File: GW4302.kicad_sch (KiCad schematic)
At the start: 75 parts, among them J1 C64, J2 microUSB, J3 JTAG, Q1 2N3904, U1 74AHC245PW, U10 74AHC125PW, U13 CH340G, U2 74AHC245PW, U3 LD1117S33, U4 74AHC245PW, U5 74AHC245PW, U6 74AHC125PW, U8 LCMXO2-640-TG100, U9 W9825G6KH-6, Y1 12M

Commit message: RFC
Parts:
- removed Q1: 2N3904, stdpads:SOT-23, symbol Transistor_BJT:MMBT3904
- R15, R4: value 10k -> 1k; LCSC Part C25804 -> C21190
- R16: value 1k -> 10k; LCSC Part C21190 -> C25804
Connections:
- net +3V3: now also U10.12 (4A); no longer R3.1
- net GND: now also R3.2; no longer U10.12 (4A), U10.13 (4~{OE})
- net JTAG~{OE}: now also R3.1, U10.11 (4Y); no longer R3.2
- net at C34.1, R16.1, R2.1: now also U10.13 (4~{OE})
- no-connect marks 10 -> 9
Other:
- title: GW4301A -> GW4302A
- moved on the sheet: C34, R2, R5, R8, U10

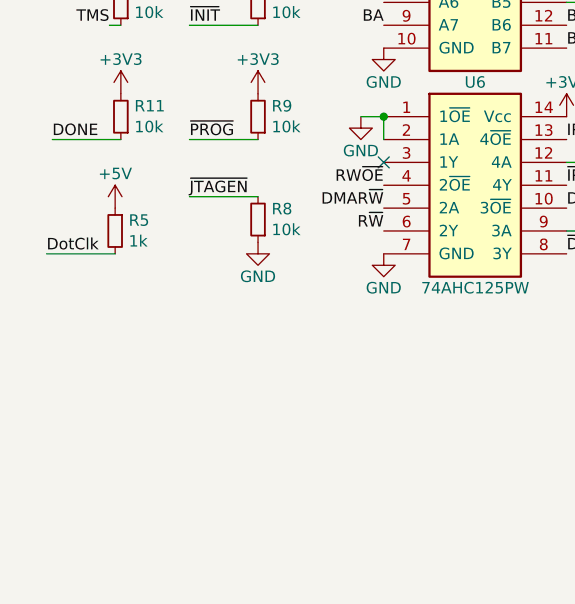
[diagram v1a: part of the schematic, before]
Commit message: Add pull-up resistors on AOE, DOE, IRQOE, RESOE
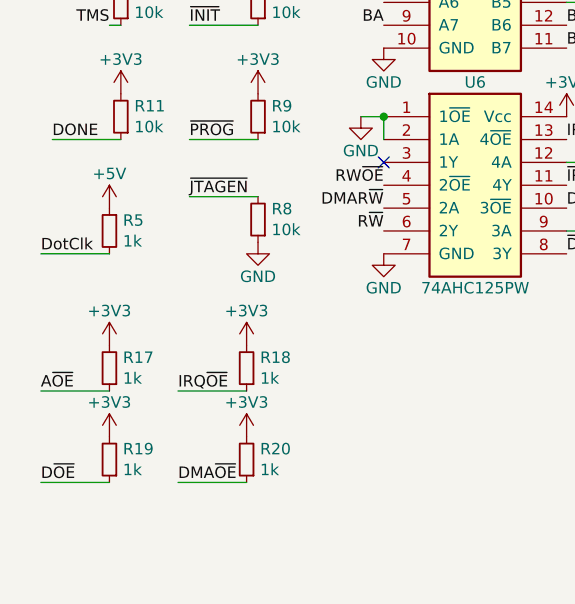
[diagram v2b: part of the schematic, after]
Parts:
- added R17, R18, R19, R20: 1k, stdpads:R_0603, symbol Device:R_Small
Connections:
- net +3V3: now also R17.2, R18.2, R19.2, R20.2
- net A~{OE}: now also R17.1
- net DMA~{OE}: now also R20.1
- net D~{OE}: now also R19.1
- net IRQ~{OE}: now also R18.1
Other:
- moved on the sheet: R5

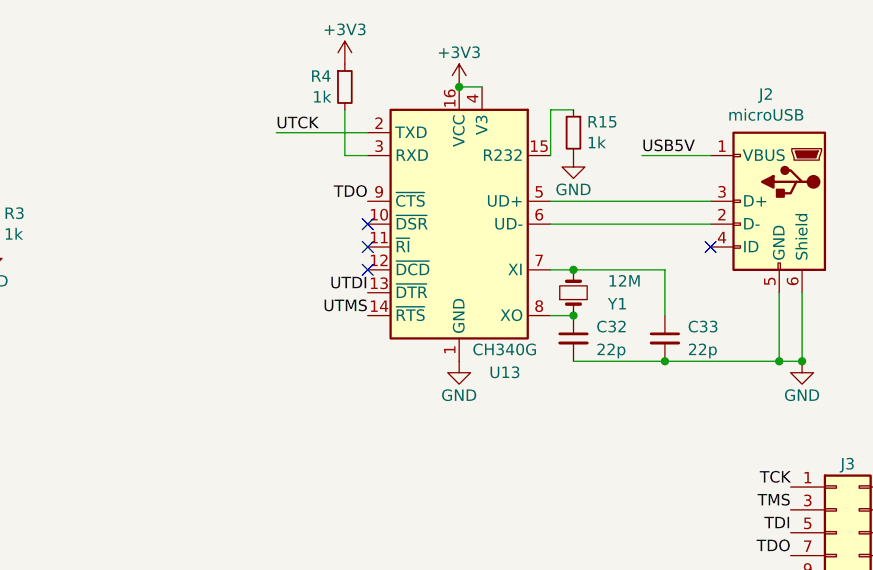
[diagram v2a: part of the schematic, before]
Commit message: Switch to 3225 crystal for USB
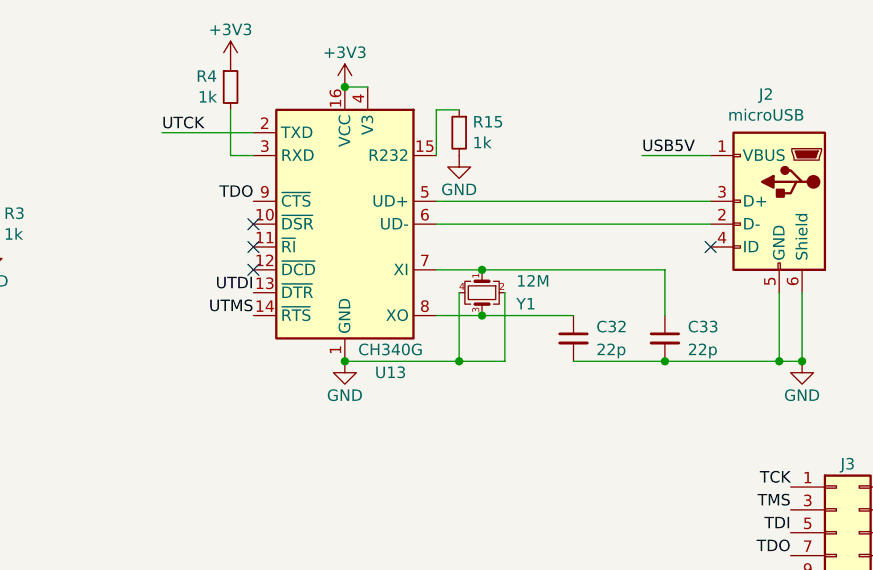
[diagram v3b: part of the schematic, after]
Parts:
- removed Y1: 12M, stdpads:Crystal_HC49-SMD, symbol Device:Crystal_Small
- added Y1: 12M, stdpads:Crystal_SMD_3225-4Pin_3.2x2.5mm, symbol Device:Crystal_GND24_Small
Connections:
- net GND: now also Y1.2, Y1.4
- net at C32.1, U13.8 (XO): now also Y1.3
- net at C33.1, U13.7 (XI): now also Y1.1
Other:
- moved on the sheet: R15, R4, U13

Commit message: Fix board ID
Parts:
- added D1: LED, stdpads:LED_0805, symbol Device:LED_Small_Filled
- added R21, R23: 1k, stdpads:R_0603, symbol Device:R_Small
- added R22: 220, stdpads:R_0805, symbol Device:R_Small
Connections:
- net +3V3: now also R21.2, R22.1, R23.1
- net RW~{OE}: now also R21.1
- net ~{LED}: now reaches U8.24 (PL7C)
- net ~{LED}: now also D1.1 (K)
- net at U13.10 (~{DSR}): now also U13.11 (~{RI}), U13.12 (~{DCD}), R23.2
- new net: D1.2 (A), R22.2
- no-connect marks 9 -> 5
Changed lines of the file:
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@@
   (junction (at 248.92 100.33) (diameter 0) (color 0 0 0 0)
   )
+  (junction (at 176.53 39.37) (diameter 0) (color 0 0 0 0)
+  )
   (junction (at 116.84 34.29) (diameter 0) (color 0 0 0 0)
   )
@@
   (junction (at 128.27 198.12) (diameter 0) (color 0 0 0 0)
   )
+  (junction (at 176.53 41.91) (diameter 0) (color 0 0 0 0)
+  )
   (junction (at 222.25 52.07) (diameter 0) (color 0 0 0 0)
   )
   (junction (at 120.65 76.2) (diameter 0) (color 0 0 0 0)
   )
-  (no_connect (at 176.53 36.83))
   (no_connect (at 50.8 156.21))
   (no_connect (at 248.92 73.66))
-  (no_connect (at 176.53 41.91))
-  (no_connect (at 176.53 39.37))
-  (no_connect (at 96.52 132.08))
   (no_connect (at 236.22 76.2))
   (no_connect (at 227.33 39.37))
@@
     (stroke (width 0) (type default) (color 0 0 0 0))
   )
+  (wire (pts (xy 151.13 64.77) (xy 153.67 64.77))
+    (stroke (width 0) (type default) (color 0 0 0 0))
+  )
   (wire (pts (xy 95.25 36.83) (xy 96.52 36.83))
     (stroke (width 0) (type default) (color 0 0 0 0))
   )
+  (wire (pts (xy 176.53 41.91) (xy 176.53 39.37))
+    (stroke (width 0) (type default) (color 0 0 0 0))
+  )
   (wire (pts (xy 218.44 130.81) (xy 228.6 130.81))
     (stroke (width 0) (type default) (color 0 0 0 0))
@@
     (stroke (width 0) (type default) (color 0 0 0 0))
   )
+  (wire (pts (xy 43.18 191.77) (xy 50.8 191.77))
+    (stroke (width 0) (type default) (color 0 0 0 0))
+  )
   (wire (pts (xy 114.3 34.29) (xy 116.84 34.29))
     (stroke (width 0) (type default) (color 0 0 0 0))
@@
     (stroke (width 0) (type default) (color 0 0 0 0))
   )
+  (wire (pts (xy 135.89 64.77) (xy 140.97 64.77))
+    (stroke (width 0) (type default) (color 0 0 0 0))
+  )
   (wire (pts (xy 204.47 44.45) (xy 204.47 52.07))
     (stroke (width 0) (type default) (color 0 0 0 0))
@@
     (stroke (width 0) (type default) (color 0 0 0 0))
   )
+  (wire (pts (xy 170.18 41.91) (xy 176.53 41.91))
+    (stroke (width 0) (type default) (color 0 0 0 0))
+  )
   (wire (pts (xy 12.7 191.77) (xy 20.32 191.77))
     (stroke (width 0) (type default) (color 0 0 0 0))
   )
+  (wire (pts (xy 176.53 36.83) (xy 176.53 39.37))
+    (stroke (width 0) (type default) (color 0 0 0 0))
+  )
   (wire (pts (xy 228.6 105.41) (xy 238.76 105.41))
     (stroke (width 0) (type default) (color 0 0 0 0))
@@
     (effects (font (size 1.27 1.27)) (justify right bottom))
   )
+  (label "~{LED}" (at 96.52 132.08 180)
+    (effects (font (size 1.27 1.27)) (justify right bottom))
+  )
   (label "RDQML" (at 191.77 144.78 0)
     (effects (font (size 1.27 1.27)) (justify left bottom))
@@
     (effects (font (size 1.27 1.27)) (justify right bottom))
   )
+  (label "RW~{OE}" (at 43.18 191.77 0)
+    (effects (font (size 1.27 1.27)) (justify left bottom))
+  )
   (label "A15" (at 50.8 59.69 180)
     (effects (font (size 1.27 1.27)) (justify right bottom))
@@
     (effects (font (size 1.27 1.27)) (justify left bottom))
   )
+  (label "~{LED}" (at 135.89 64.77 0)
+    (effects (font (size 1.27 1.27)) (justify left bottom))
+  )
   (label "D~{OE}" (at 12.7 191.77 0)
     (effects (font (size 1.27 1.27)) (justify left bottom))
@@
     (pin "1")
   )
+  (symbol (lib_id "Device:R_Small") (at 148.59 64.77 270) (unit 1)
+    (in_bom yes) (on_board yes)
+    (property "Reference" "R22" (id 0) (at 148.59 60.96 90))
+    (property "Value" "220" (id 1) (at 148.59 63.5 90)
+      (effects (font (size 1.27 1.27)) (justify bottom))
+    )
+    (property "Footprint" "stdpads:R_0805" (id 2) (at 148.59 64.77 0)
+      (effects (font (size 1.27 1.27)) hide)
+    )
+    (property "Datasheet" "~" (id 3) (at 148.59 64.77 0)
+      (effects (font (size 1.27 1.27)) hide)
+    )
+    (property "LCSC Part" "" (id 4) (at 148.59 64.77 0)
+      (effects (font (size 1.27 1.27)) hide)
+    )
+    (pin "1")
+    (pin "2")
+  )
+  (symbol (lib_id "power:+3V3") (at 170.18 36.83 0) (mirror y) (unit 1)
+    (in_bom yes) (on_board yes)
+    (property "Reference" "#PWR0166" (id 0) (at 170.18 40.64 0)
+      (effects (font (size 1.27 1.27)) hide)
+    )
+    (property "Value" "+3V3" (id 1) (at 170.18 33.02 0))
+    (property "Footprint" "" (id 2) (at 170.18 36.83 0)
+      (effects (font (size 1.27 1.27)) hide)
+    )
+    (property "Datasheet" "" (id 3) (at 170.18 36.83 0)
+      (effects (font (size 1.27 1.27)) hide)
+    )
+    (pin "1")
+  )
   (symbol (lib_id "Device:R_Small") (at 173.99 21.59 0) (unit 1)
     (in_bom yes) (on_board yes)
@@
     (pin "2")
   )
+  (symbol (lib_id "Device:R_Small") (at 50.8 189.23 180) (unit 1)
+    (in_bom yes) (on_board yes)
+    (property "Reference" "R21" (id 0) (at 52.2986 188.0616 0)
+      (effects (font (size 1.27 1.27)) (justify right))
+    )
+    (property "Value" "1k" (id 1) (at 52.2986 190.373 0)
+      (effects (font (size 1.27 1.27)) (justify right))
+    )
+    (property "Footprint" "stdpads:R_0603" (id 2) (at 50.8 189.23 0)
+      (effects (font (size 1.27 1.27)) hide)
+    )
+    (property "Datasheet" "~" (id 3) (at 50.8 189.23 0)
+      (effects (font (size 1.27 1.27)) hide)
+    )
+    (property "LCSC Part" "C25804" (id 4) (at 50.8 189.23 0)
+      (effects (font (size 1.27 1.27)) hide)
+    )
+    (pin "1")
+    (pin "2")
+  )
+  (symbol (lib_id "power:+3V3") (at 153.67 64.77 0) (unit 1)
+    (in_bom yes) (on_board yes)
+    (property "Reference" "#PWR0165" (id 0) (at 153.67 68.58 0)
+      (effects (font (size 1.27 1.27)) hide)
+    )
+    (property "Value" "+3V3" (id 1) (at 153.67 60.96 0))
+    (property "Footprint" "" (id 2) (at 153.67 64.77 0)
+      (effects (font (size 1.27 1.27)) hide)
+    )
+    (property "Datasheet" "" (id 3) (at 153.67 64.77 0)
+      (effects (font (size 1.27 1.27)) hide)
+    )
+    (pin "1")
+  )
   (symbol (lib_id "Device:R_Small") (at 20.32 189.23 180) (unit 1)
     (in_bom yes) (on_board yes)
@@
     (pin "4")
   )
+  (symbol (lib_id "Device:R_Small") (at 170.18 39.37 0) (unit 1)
+    (in_bom yes) (on_board yes)
+    (property "Reference" "R23" (id 0) (at 168.6814 38.2016 0)
+      (effects (font (size 1.27 1.27)) (justify right))
+    )
+    (property "Value" "1k" (id 1) (at 168.6814 40.513 0)
+      (effects (font (size 1.27 1.27)) (justify right))
+    )
+    (property "Footprint" "stdpads:R_0603" (id 2) (at 170.18 39.37 0)
+      (effects (font (size 1.27 1.27)) hide)
+    )
+    (property "Datasheet" "~" (id 3) (at 170.18 39.37 0)
+      (effects (font (size 1.27 1.27)) hide)
+    )
+    (property "LCSC Part" "C21190" (id 4) (at 170.18 39.37 0)
+      (effects (font (size 1.27 1.27)) hide)
+    )
+    (pin "1")
+    (pin "2")
+  )
   (symbol (lib_id "power:GND") (at 96.52 41.91 0) (mirror y) (unit 1)
     (in_bom yes) (on_board yes)
@@
     (pin "1")
   )
+  (symbol (lib_id "Device:LED_Small_Filled") (at 143.51 64.77 0) (unit 1)
+    (in_bom yes) (on_board yes)
+    (property "Reference" "D1" (id 0) (at 143.51 62.23 0))
+    (property "Value" "LED" (id 1) (at 143.51 66.04 0)
+      (effects (font (size 1.27 1.27)) (justify top))
+    )
+    (property "Footprint" "stdpads:LED_0805" (id 2) (at 143.51 64.77 90)
+      (effects (font (size 1.27 1.27)) hide)
+    )
+    (property "Datasheet" "~" (id 3) (at 143.51 64.77 90)
+      (effects (font (size 1.27 1.27)) hide)
+    )
+    (pin "1")
+    (pin "2")
+  )
   (symbol (lib_id "Device:R_Small") (at 199.39 26.67 0) (mirror y) (unit 1)
     (in_bom yes) (on_board yes)
@@
     (pin "2")
   )
+  (symbol (lib_id "power:+3V3") (at 50.8 186.69 0) (unit 1)
+    (in_bom yes) (on_board yes)
+    (property "Reference" "#PWR0164" (id 0) (at 50.8 190.5 0)
+      (effects (font (size 1.27 1.27)) hide)
+    )
+    (property "Value" "+3V3" (id 1) (at 50.8 182.88 0))
+    (property "Footprint" "" (id 2) (at 50.8 186.69 0)
+      (effects (font (size 1.27 1.27)) hide)
+    )
+    (property "Datasheet" "" (id 3) (at 50.8 186.69 0)
+      (effects (font (size 1.27 1.27)) hide)
+    )
+    (pin "1")
+  )
   (symbol (lib_id "power:+3V3") (at 35.56 176.53 0) (unit 1)
     (in_bom yes) (on_board yes)
@@
       (reference "#PWR0163") (unit 1) (value "GND") (footprint "")
     )
+    (path "/e9037073-a260-40e3-be0e-cefe6ac6dda9"
+      (reference "#PWR0164") (unit 1) (value "+3V3") (footprint "")
+    )
+    (path "/73894dbb-be06-4c9d-b554-a3676ed6b03f"
+      (reference "#PWR0165") (unit 1) (value "+3V3") (footprint "")
+    )
+    (path "/6686fd86-c321-4afa-a380-180b1d365c63"
+      (reference "#PWR0166") (unit 1) (value "+3V3") (footprint "")
+    )
     (path "/00000000-0000-0000-0000-000061e4aaea"
       (reference "#PWR0204") (unit 1) (value "GND") (footprint "")
@@
       (reference "C35") (unit 1) (value "2u2") (footprint "stdpads:C_0603")
     )
+    (path "/b9ae8c5a-035f-41ae-8bc2-d12da2f7ee33"
+      (reference "D1") (unit 1) (value "LED") (footprint "stdpads:LED_0805")
+    )
     (path "/00000000-0000-0000-0000-00005cc4f6a4"
       (reference "FID1") (unit 1) (value "Fiducial") (footprint "stdpads:Fiducial")
@@
       (reference "R20") (unit 1) (value "1k") (footprint "stdpads:R_0603")
     )
+    (path "/67194e79-e6ef-4afa-b627-22a748843aa9"
+      (reference "R21") (unit 1) (value "1k") (footprint "stdpads:R_0603")
+    )
+    (path "/663d8eed-3e10-4cda-bb40-d938d59731ed"
+      (reference "R22") (unit 1) (value "220") (footprint "stdpads:R_0805")
+    )
+    (path "/abdcf946-05da-4243-8218-76e87ac06aad"
+      (reference "R23") (unit 1) (value "1k") (footprint "stdpads:R_0603")
+    )
     (path "/00000000-0000-0000-0000-000061d1ea13"

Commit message: Done?
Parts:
- removed R15, R23, R4: 1k, stdpads:R_0603, symbol Device:R_Small
- added C36: 2u2, stdpads:C_0603, symbol Device:C_Small
- H3, H4, H5: symbol Mechanical:MountingHole_Pad -> Mechanical:MountingHole
- J2: footprint stdpads:USB_Micro-B_ShouHan_MicroXNJ -> stdpads:USB_Micro-B_Amphenol_10118192-0001
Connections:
- net +3V3: now also U13.10 (~{DSR}), U13.11 (~{RI}), U13.12 (~{DCD}), U13.3 (RXD)
- net GND: now also U13.15 (R232), C36.2; no longer H3.1, H4.1, H5.1
- net USB5V: now also C36.1

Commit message: New version
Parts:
- removed U10: 74AHC125PW, stdpads:TSSOP-14_4.4x5mm_P0.65mm, symbol GW_Logic:74125
- removed U3: LD1117S33, stdpads:SOT-223, symbol Regulator_Linear:LD1117S33TR_SOT223
- added C32, C33, C40, C7: 2u2, stdpads:C_0603, symbol Device:C_Small
- added J4: BTN, stdpads:PinHeader_1x03_P2.00mm_Vertical, symbol Connector_Generic:Conn_01x03
- added R15, R27: 3k3, stdpads:R_0603, symbol Device:R_Small
- added R23, R25: DNP, stdpads:R_0603, symbol Device:R_Small
- added R24, R26: 47, stdpads:R_0603, symbol Device:R_Small
- added R28: 1k, stdpads:R_0603, symbol Device:R_Small
- added R4: 10k, stdpads:R_0603, symbol Device:R_Small
- added U14: 74LVC1G17GW, stdpads:SOT-353, symbol GW_Logic:741G07GW
- added U15: XC6206P332MR, stdpads:SOT-23, symbol Regulator_Linear:XC6206PxxxMR
- added U16: LM66200DRL, stdpads:SOT-583, symbol GW_Power:LM66200DCK
- added U3: W25Q128JVSIQ, stdpads:SOIC-8_5.3mm, symbol GW_RAM:SPIFlash-SO-8
- added U5: 74AHCT125PW, stdpads:TSSOP-14_4.4x5mm_P0.65mm, symbol GW_Logic:74125
- added U7, U8, U9: 74AHCT573PW, stdpads:TSSOP-20_4.4x6.5mm_P0.65mm, symbol GW_Logic:74573
- C1, C2, C3, C4, C5, C6: value 10u -> 2u2; footprint stdpads:C_0805 -> stdpads:C_0603; LCSC Part C15850 -> C23630
- C10, C11, C12, C9: value 2u2 -> 10u; footprint stdpads:C_0603 -> stdpads:C_0805; LCSC Part C23630 -> C15850
- C34: value 22p -> 2u2; LCSC Part C1653 -> C23630
- D1: LCSC Part (none) -> C284932
- H1, H2, H3, H4, H5: value (none) -> ~
- J2: LCSC Part C404969 -> C132564
- J3: footprint Connector:Tag-Connect_TC2050-IDC-FP_2x05_P1.27mm_Vertical -> stdpads:Tag-Connect_TC2050-IDC-FP_2x05_P1.27mm_Vertical
- R16: value 10k -> 3k3; LCSC Part C25804 -> C22978
- R17, R18, R19, R20: value 1k -> 3k3; LCSC Part C25804 -> C22978
- R2: value 1k -> 47; LCSC Part C21190 -> C23182
- R21: value 1k -> 47; LCSC Part C25804 -> C23182
- R22: LCSC Part (none) -> C17557
- R3: value 1k -> 10k; LCSC Part C21190 -> C25804
- R8: value 10k -> DNP; LCSC Part C25804 -> (none)
- U1: renamed from U8; LCSC Part (none) -> C1521611
- U10: renamed from U1; value 74AHC245PW -> 74LVC245APW; LCSC Part C132987 -> C7848
- U11: renamed from U2; value 74AHC245PW -> 74LVC245APW; LCSC Part C132987 -> C7848
- U12: renamed from U4; value 74AHC245PW -> 74LVC245APW; LCSC Part C132987 -> C7848
- U4: renamed from U6; value 74AHC125PW -> 74AHCT125PW; LCSC Part C129518 -> C36365
- U6: renamed from U5; value 74AHC245PW -> 74LVC245APW; LCSC Part C132987 -> C7848
- Y1: LCSC Part (none) -> C9002
- renumbered C32 to C37, C33 to C38, C7 to C39, U9 to U2
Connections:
- net RESET~{OE} is gone; now on an unnamed net: U1.19 (PL6D)
- net ~{PROG} is gone; now on net ~{LED}: R9.1, U1.81 (~{PROGRAM}/PT10D)
- net +3V3: now also C34.1, C36.1, D1.2 (A), R16.2, R3.2, U1.11 ((VccIO3)), C32.1, C33.1, C40.1, J4.2 (Pin_2), R15.2, R27.2, R4.2, U14.5 (Vcc), U15.2 (VO), U3.8 (Vcc), U7.11 (LE), U8.11 (LE); no longer C10.1, C3.1, C4.1, C5.1, C6.1, C8.1, C9.1, R21.2, R22.1, U13.3 (RXD), U4.14 (Vcc)
- net +5V: now also C10.1, C9.1, U15.3 (VI), U16.2 (Vout), U16.7 (Vout); no longer C1.1, C2.1, J1.2 (Pin_2), J1.3 (Pin_3), R5.1
- net A0: now also U11.11 (B7), U8.19 (Q0); no longer U10.9 (A7)
- net A1: now also U11.12 (B6), U8.18 (Q1); no longer U10.8 (A6)
- net A10: now also U10.13 (B5), U7.17 (Q2); no longer U11.7 (A5)
- net A11: now also U10.14 (B4), U7.16 (Q3); no longer U11.6 (A4)
- net A12: now also U10.15 (B3), U7.15 (Q4); no longer U11.5 (A3)
- net A13: now also U10.16 (B2), U7.14 (Q5); no longer U11.4 (A2)
- net A14: now also U10.17 (B1), U7.13 (Q6); no longer U11.3 (A1)
- net A15: now also U10.18 (B0), U7.12 (Q7); no longer U11.2 (A0)
- net A2: now also U11.13 (B5), U8.17 (Q2); no longer U10.7 (A5)
- net A3: now also U11.14 (B4), U8.16 (Q3); no longer U10.6 (A4)
- net A4: now also U11.15 (B3), U8.15 (Q4); no longer U10.5 (A3)
- net A5: now also U11.16 (B2), U8.14 (Q5); no longer U10.4 (A2)
- net A6: now also U11.17 (B1), U8.13 (Q6); no longer U10.3 (A1)
- net A7: now also U11.18 (B0), U8.12 (Q7); no longer U10.2 (A0)
- net A8: now also U10.11 (B7), U7.19 (Q0); no longer U11.9 (A7)
- net A9: now also U10.12 (B6), U7.18 (Q1); no longer U11.8 (A6)
- net BA0: now also U1.68 (PR3B), U11.9 (A7), U8.2 (D0); no longer U1.51 (PR7D), U10.11 (B7)
- net BA1: now also U1.70 (PR2D), U11.8 (A6), U8.3 (D1); no longer U1.52 (PR7C), U10.12 (B6)
- net BA10: now also U1.67 (PR3C), U10.7 (A5), U7.4 (D2); no longer U1.39 (PB10D/PCLKC2_1), U11.13 (B5)
- net BA11: now also U1.65 (PR5A), U10.6 (A4), U7.5 (D3); no longer U1.37 (PB10B), U11.14 (B4)
- net BA12: now also U1.63 (PCLKT1_0/PR5C), U10.5 (A3), U7.6 (D4); no longer U1.36 (PB10A), U11.15 (B3)
- net BA13: now also U1.3 (PL2C/PCLKT3_2), U10.4 (A2), U7.7 (D5); no longer U1.42 (PB12C), U11.16 (B2)
- net BA14: now also U1.2 (PL2B), U10.3 (A1), U7.8 (D6); no longer U1.40 (PB12A), U11.17 (B1)
- net BA15: now also U1.1 (PL2A), U10.2 (A0), U7.9 (D7); no longer U1.35 (PB6D/PCLKC_0), U11.18 (B0)
- net BA2: now also U1.71 (PR2C), U11.7 (A5), U8.4 (D2); no longer U1.54 (PR7A), U10.13 (B5)
- net BA3: now also U1.66 (PR3D), U11.6 (A4), U8.5 (D3); no longer U1.53 (PR7B), U10.14 (B4)
- net BA4: now also U1.64 (PR5B), U11.5 (A3), U8.6 (D4); no longer U1.45 (PB14A), U10.15 (B3)
- net BA5: now also U1.62 (PCLKC1_0/PR5D), U11.4 (A2), U8.7 (D5); no longer U1.49 (PB14D/SI/SISPI), U10.16 (B2)
- net BA6: now also U1.58 (PR6C), U11.3 (A1), U8.8 (D6); no longer U1.47 (PB14), U10.17 (B1)
- net BA7: now also U1.59 (PR6B), U11.2 (A0), U8.9 (D7); no longer U1.48 (PB14C/SN), U10.18 (B0)
- net BA8: now also U1.69 (PR3A), U10.9 (A7), U7.2 (D0); no longer U1.43 (PB12D), U11.11 (B7)
- net BA9: now also U1.60 (PR6A), U10.8 (A6), U7.3 (D1); no longer U1.41 (PB12B), U11.12 (B6)
- net BBA: now also U1.99 (PT6A); no longer U1.30 (PB4D)
- net BD0: now also U1.10 (PL3D), U12.9 (A7), U2.2 (DQ0), U2.53 (DQ15), U9.2 (D0); no longer U1.4 (PL2D/PCLKC3_2), U12.11 (B7)
- net BD1: now also U1.12 (PL5A/PCLKT3_1), U12.8 (A6), U2.4 (DQ1), U2.51 (DQ14), U9.3 (D1); no longer U1.7 (PL3A), U12.12 (B6)
- net BD2: now also U1.13 (PL5B/PCLKC3_1), U12.7 (A5), U2.5 (DQ2), U2.50 (DQ13), U9.4 (D2); no longer U1.8 (PL3B), U12.13 (B5)
- net BD3: now also U1.14 (PL5C), U12.6 (A4), U2.48 (DQ12), U2.7 (DQ3), U9.5 (D3); no longer U1.10 (PL3D), U12.14 (B4)
- net BD4: now also U1.15 (PL5D), U12.5 (A3), U2.47 (DQ11), U2.8 (DQ4), U9.6 (D4); no longer U1.9 (PL3C), U12.15 (B3)
- net BD5: now also U1.16 (PL6A), U12.4 (A2), U2.10 (DQ5), U2.45 (DQ10), U9.7 (D5); no longer U1.12 (PL5A/PCLKT3_1), U12.16 (B2)
- net BD6: now also U1.17 (PL6B), U12.3 (A1), U2.11 (DQ6), U2.44 (DQ9), U9.8 (D6); no longer U1.14 (PL5C), U12.17 (B1)
- net BD7: now also U1.18 (PL6C), U12.2 (A0), U2.13 (DQ7), U2.42 (DQ8), U9.9 (D7); no longer U1.13 (PL5B/PCLKC3_1), U12.18 (B0)
- net BPHI2: now also U1.88 (PCLKT0_1/PT9A); no longer U1.38 (PB10C/PCLKT2_1)
- net BR~{W}: now also U1.85 (SDA/PCLKC0_0/PT9D), U6.17 (B1); no longer U1.21 (PL7B/PCLKC3_0), U6.16 (B2)
- net C8M: now also U1.86 (SCL/PCLKT0_0/PT9C); no longer U1.34 (PB6C/PCLKT2_0)
- net D0: now also U12.11 (B7), U9.19 (Q0); no longer U12.9 (A7)
- net D1: now also U12.12 (B6), U9.18 (Q1); no longer U12.8 (A6)
- net D2: now also U12.13 (B5), U9.17 (Q2); no longer U12.7 (A5)
- net D3: now also U12.14 (B4), U9.16 (Q3); no longer U12.6 (A4)
- net D4: now also U12.15 (B3), U9.15 (Q4); no longer U12.5 (A3)
- net D5: now also U12.16 (B2), U9.14 (Q5); no longer U12.4 (A2)
- net D6: now also U12.17 (B1), U9.13 (Q6); no longer U12.3 (A1)
- net D7: now also U12.18 (B0), U9.12 (Q7); no longer U12.2 (A0)
- net DONE: now also U5.1 (1~{OE})
- net GND: now also U10.1 (AtoB), U11.1 (AtoB), U12.1 (AtoB), U2.19 (~{CS}), U4.11 (4Y), U4.13 (4~{OE}), U4.5 (2A), C32.2, C33.2, C40.2, C7.2, J4.3 (Pin_3), U14.3 (GND), U15.1 (GND), U16.1 (GND), U16.4 (~{ON}), U16.5 (GND), U3.4 (GND), U5.12 (4A), U5.2 (1A), U5.5 (2A), U5.7 (GND), U7.10 (GND), U8.10 (GND), U9.10 (GND); no longer R16.2, R3.2, R8.1, U4.1 (1~{OE}), U6.17 (B1), U6.3 (A1)
- net PHI2: now also U6.6 (A4); no longer U6.7 (A5)
- net RA0: now also U1.45 (PB14A); no longer U1.99 (PT6A)
- net RA1: now also U1.43 (PB12D); no longer U1.1 (PL2A)
- net RA10: now also U1.53 (PR7B); no longer U1.98 (PT6B)
- net RA11: now also U1.34 (PB6C/PCLKT2_0); no longer U1.69 (PR3A)
- net RA12: now also U1.36 (PB10A); no longer U1.68 (PR3B)
- net RA2: now also U1.42 (PB12C); no longer U1.2 (PL2B)
- net RA3: now also U1.41 (PB12B); no longer U1.3 (PL2C/PCLKT3_2)
- net RA4: now also U1.40 (PB12A); no longer R8.2, U1.82 (~{JTAGEN}/PT10C)
- net RA5: now also U1.39 (PB10D/PCLKC2_1); no longer U1.78 (PT11A)
- net RA6: now also U1.38 (PB10C/PCLKT2_1); no longer U1.75 (PR2A)
- net RA7: now also U1.35 (PB6D/PCLKC_0); no longer U1.74 (PR2B)
- net RA8: now also U1.31 (PB6A/MCLK/CCLK); no longer U1.71 (PR2C)
- net RA9: now also U1.32 (PB6B/SO/SPISO); no longer U1.70 (PR2D)
- net RBA0: now also U1.48 (PB14C/SN); no longer U1.96 (PT6D)
- net RBA1: now also U1.47 (PB14); no longer U1.97 (PT6C)
- net RCKE: now also U1.37 (PB10B); no longer U1.67 (PR3C)
- net RDQMH: now also U1.52 (PR7C); no longer U1.83 (PT10B)
- net RDQML: now also U1.57 (PR6D); no longer U1.84 (PT10A)
- net R~{WE}: now also U1.51 (PR7D); no longer U1.85 (SDA/PCLKC0_0/PT9D)
- net R~{W}: now also U6.3 (A1), U5.8 (3Y); no longer U4.6 (2Y), U6.4 (A2)
- net TCK: now also R2.1, U1.91 (TCK/PT7C), R23.1; no longer J3.1 (Pin_1), R10.2
- net TDI: now also R25.1, R26.1; no longer J3.5 (Pin_5)
- net TMS: now also R8.1, R24.1; no longer J3.3 (Pin_3), R14.1
- net UTDI: now also R26.2
- net UTMS: now also R24.2
- net ~{CAS}: now also U1.54 (PR7A); no longer U1.86 (SCL/PCLKT0_0/PT9C)
- net ~{DMA}: now also U5.11 (4Y); no longer U4.8 (3Y)
- net ~{EXROM}: now also U5.6 (2Y)
- net ~{GAME}: now also U5.3 (1Y)
- net ~{IO2}: now also U6.7 (A5); no longer U6.8 (A6)
- net ~{IRQ}: now also U4.6 (2Y); no longer U4.11 (4Y)
- net ~{LED}: now also R22.2; no longer D1.1 (K), U1.24 (PL7C)
- net ~{NMI}: now also U4.8 (3Y)
- net ~{RAS}: now also U1.49 (PB14D/SI/SISPI); no longer U1.87 (PT9B/PCLKC0_1)
- net ~{ROMH}: now also U6.4 (A2)
- net ~{ROML}: now also U6.8 (A6)
- net at R1.2: now also U6.14 (B4); no longer U6.13 (B5)
- net ~{RES}: now reaches U4.3 (1Y)
- net ~{RES}: now also J1.42 (Pin_42), U14.2 (A)
- net at R7.2: no longer U1.63 (PCLKT1_0/PR5C)
- removed net ADIR: U1.31 (PB6A/MCLK/CCLK), U10.1 (AtoB), U11.1 (AtoB)
- net A~{OE} renamed Ain~{OE}
- net Ain~{OE}: now also U1.4 (PL2D/PCLKC3_2); no longer R17.1, U1.32 (PB6B/SO/SPISO)
- net B~{IO1} renamed B~{IO}1
- net B~{IO}1: now also U1.96 (PT6D); no longer U1.27 (PB4A/CSSPIN)
- net B~{IO2} renamed B~{ROML}
- net B~{ROML}: now also U1.97 (PT6C); no longer U1.29 (PB4C)
- net B~{RESET} renamed B~{RES}
- net B~{RES}: now also U14.4 (Y); no longer U6.14 (B4)
- removed net DDIR: U1.15 (PL5D), U12.1 (AtoB)
- removed net DMAR~{W}: U1.17 (PL6B), U4.5 (2A)
- removed net DMA~{OE}: R20.1, U1.25 (PL7D), U4.10 (3~{OE})
- removed net D~{OE}: R19.1, U1.16 (PL6A), U12.19 (~{OE})
- removed net IRQ~{OE}: R18.1, U1.18 (PL6C), U4.13 (4~{OE})
- net JTAG~{OE} renamed F~{WP}
- net F~{WP}: now also U3.3 (~{WP}/IO2)
- removed net RD0: U1.57 (PR6D), U2.2 (DQ0), U2.53 (DQ15)
- removed net RD1: U1.58 (PR6C), U2.4 (DQ1), U2.51 (DQ14)
- removed net RD2: U1.59 (PR6B), U2.5 (DQ2), U2.50 (DQ13)
- removed net RD3: U1.60 (PR6A), U2.48 (DQ12), U2.7 (DQ3)
- removed net RD4: U1.62 (PCLKC1_0/PR5D), U2.47 (DQ11), U2.8 (DQ4)
- removed net RD5: U1.64 (PR5B), U2.10 (DQ5), U2.45 (DQ10)
- removed net RD6: U1.65 (PR5A), U2.11 (DQ6), U2.44 (DQ9)
- removed net RD7: U1.66 (PR3D), U2.13 (DQ7), U2.42 (DQ8)
- removed net RW~{OE}: R21.1, U1.20 (PL7A/PCLKT3_0), U4.4 (2~{OE})
- removed net R~{CS}: U1.88 (PT9A/PCLKT0_1), U2.19 (~{CS})
- net TCKr renamed CTCK
- net CTCK: now also R23.2; no longer U1.91 (TCK/PT7C)
- removed net USB5V: C36.1, J2.1 (VBUS), R2.2
- net UTCK renamed UTXD
- net UTXD: now also R2.2, R28.1
- net ~{INIT} renamed O~{EXROM}
- net O~{EXROM}: now also U5.4 (2~{OE})
- removed net ~{RESET}: J1.42 (Pin_42), U6.6 (A4)
- new net: D1.1 (K), R22.1
- new net Aout~{OE}: R17.1, U1.83 (PT10B), U5.10 (3~{OE}), U7.1 (~{OE}), U8.1 (~{OE})
- new net B~{IO}2: U1.98 (PT6B), U6.13 (B5)
- new net B~{ROMH}: U1.87 (PCLKC0_1/PT9B), U6.16 (B2)
- new net C5V: C1.1, C2.1, C3.1, C4.1, C5.1, C6.1, J1.2 (Pin_2), J1.3 (Pin_3), R5.1, U16.3 (Vin1), U4.14 (Vcc), U5.14 (Vcc), U7.20 (Vcc), U8.20 (Vcc), U9.20 (Vcc)
- new net CTCKr: J3.1 (Pin_1), R10.2
- new net CTDI: J3.5 (Pin_5), R25.2
- new net CTMS: J3.3 (Pin_3), R14.1, R8.2
- new net DLE: U1.8 (PL3B), U9.11 (LE)
- new net Din~{OE}: U1.9 (PL3C), U12.19 (~{OE})
- new net Dout~{OE}: R19.1, U1.7 (PL3A), U9.1 (~{OE})
- new net FMISO: U1.20 (PL7A/PCLKT3_0), U3.2 (DO/IO1)
- new net FMOSI: U1.24 (PL7C), U3.5 (DI/IO0)
- new net FRXD: R28.2, U1.29 (PB4C)
- new net FSCK: R21.2, U3.6 (CLK)
- new net FSCKr: R21.1, U1.25 (PL7D)
- new net FTXD: U1.27 (PB4A/CSSPIN), U13.3 (RXD)
- new net F~{CS}: U1.21 (PL7B/PCLKC3_0), U3.1 (~{CS})
- new net F~{HLD}: R4.1, U3.7 (~{HLD}/IO3)
- new net OR~{W}: U1.84 (PT10A), U5.9 (3A)
- new net O~{DMA}: R20.1, U1.82 (JTAGEN/PT10C), U5.13 (4~{OE})
- new net O~{IRQ}: R18.1, U1.75 (PR2A), U4.4 (2~{OE})
- new net O~{NMI}: R16.1, U1.78 (PT11A), U4.10 (3~{OE})
- new net O~{RES}: R15.1, U1.74 (PR2B), U4.1 (1~{OE})
- new net U5V: C7.1, C8.1, J2.1 (VBUS), U16.6 (Vin2)
- new net ~{BTN}: J4.1 (Pin_1), R27.1, U1.30 (PB4D)
- no-connect marks 5 -> 9
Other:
- moved on the sheet: C37, C38, C39, D1, FID1, FID2, FID3, FID4, H1, H2, H3, H4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
